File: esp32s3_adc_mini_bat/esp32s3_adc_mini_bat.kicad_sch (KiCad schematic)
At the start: 0 parts

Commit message: feat: ES8388
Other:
- sheet ADC renamed CODEC
- sheet CODEC: file ADC.kicad_sch -> CODEC.kicad_sch
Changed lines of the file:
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@@
 		)
 		(instances
-			(project "esp32s3_adc_mini"
+			(project "esp32s3_adc_mini_bat"
 				(path "/653e6366-f1a6-41e9-883c-109905f9b5fe"
 					(page "3")
@@
 		)
 		(instances
-			(project "esp32s3_adc_mini"
+			(project "esp32s3_adc_mini_bat"
 				(path "/653e6366-f1a6-41e9-883c-109905f9b5fe"
 					(page "4")
@@
 		)
 		(instances
-			(project "esp32s3_adc_mini"
+			(project "esp32s3_adc_mini_bat"
 				(path "/653e6366-f1a6-41e9-883c-109905f9b5fe"
 					(page "5")
@@
 			(color 0 0 0 0)
 		)
-		(property "Sheetname" "ADC"
+		(property "Sheetname" "CODEC"
 			(at 212.09 48.8184 0)
 			(show_name no)
@@
 			)
 		)
-		(property "Sheetfile" "ADC.kicad_sch"
+		(property "Sheetfile" "CODEC.kicad_sch"
 			(at 212.09 81.8646 0)
 			(show_name no)
@@
 		)
 		(instances
-			(project "esp32s3_adc_mini"
+			(project "esp32s3_adc_mini_bat"
 				(path "/653e6366-f1a6-41e9-883c-109905f9b5fe"
 					(page "7")
@@
 		)
 		(instances
-			(project "esp32s3_adc_mini"
+			(project "esp32s3_adc_mini_bat"
 				(path "/653e6366-f1a6-41e9-883c-109905f9b5fe"
 					(page "2")
@@
 		)
 		(instances
-			(project "esp32s3_adc_mini"
+			(project "esp32s3_adc_mini_bat"
 				(path "/653e6366-f1a6-41e9-883c-109905f9b5fe"
 					(page "6")
@@
 		)
 		(instances
-			(project "esp32s3_adc_mini"
+			(project "esp32s3_adc_mini_bat"
 				(path "/653e6366-f1a6-41e9-883c-109905f9b5fe"
 					(page "8")

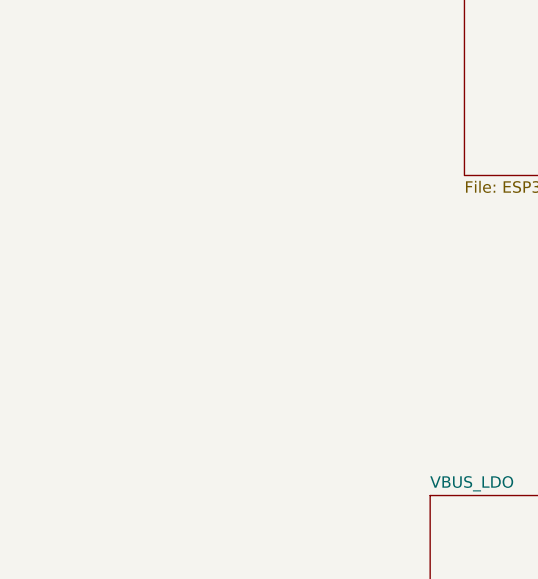
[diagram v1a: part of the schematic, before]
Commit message: feat: schematic done and pcb grouping
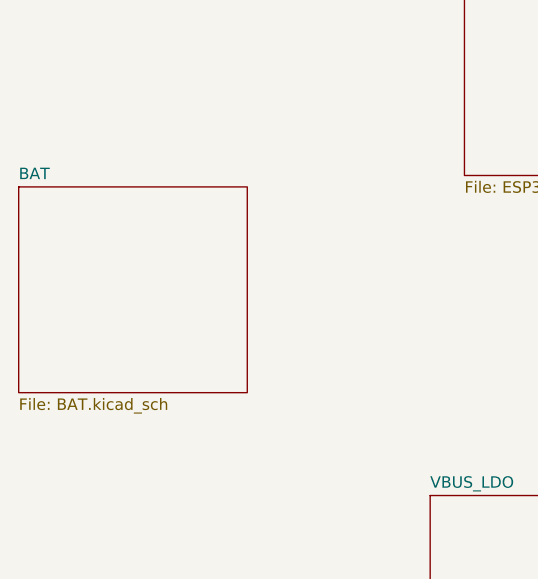
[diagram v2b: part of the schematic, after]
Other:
- added sheet BAT (BAT.kicad_sch)
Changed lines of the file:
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@@
+	)
+	(sheet
+		(at 26.67 93.98)
+		(size 25.4 22.86)
+		(exclude_from_sim no)
+		(in_bom yes)
+		(on_board yes)
+		(dnp no)
+		(fields_autoplaced yes)
+		(stroke
+			(width 0.1524)
+			(type solid)
+		)
+		(fill
+			(color 0 0 0 0)
+		)
+		(property "Sheetname" "BAT"
+			(at 26.67 93.2684 0)
+			(show_name no)
+			(do_not_autoplace no)
+			(effects
+				(font
+					(size 1.27 1.27)
+				)
+				(justify left bottom)
+			)
+		)
+		(property "Sheetfile" "BAT.kicad_sch"
+			(at 26.67 117.4246 0)
+			(show_name no)
+			(do_not_autoplace no)
+			(effects
+				(font
+					(size 1.27 1.27)
+				)
+				(justify left top)
+			)
+		)
+		(instances
+			(project "esp32s3_adc_mini_bat"
+				(path "/653e6366-f1a6-41e9-883c-109905f9b5fe"
+					(page "9")
+				)
+			)
+		)
 	)
 	(sheet
